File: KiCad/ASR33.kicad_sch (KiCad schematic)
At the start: 45 parts, among them J1 USB-C, J2 DC, J3 Power, J4 RUN, J5 Tx, J6 Rx, Q1 NX7002AK, SW1 SW_Push, U1 FT231XQ, U2 ESP32-WROOM-32, U3 NCR402U, U4 NCR402U, U5 LTV-356T, U6 LMR16006+FB, U7 QR

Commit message: New PICO version
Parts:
- removed JP1, JP2, JP4: 20R NF, RevK:Pad_1206_0805_Open, symbol Jumper:SolderJumper_2_Open
- removed JP3: GND-Linked, RevK:Pad_1206_0805_Bridged, symbol Jumper:SolderJumper_2_Bridged
- removed U2: ESP32-WROOM-32, RevK:ESP32-WROOM-32, symbol RevK:ESP32-WROOM-32
- added U1: ESP32-PICO-MINI-02, RevK:ESP32-PICO-MINI-02, symbol RevK:ESP32-PICO-MINI-02
- renumbered U1 to U2
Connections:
- net +3V3: now also U1.3 (3V3)
- net B: now also U1.15 (IO25)
- net BUTTON: now also U1.26 (IO20)
- net EN: now also U1.8 (EN)
- net G: now also U1.13 (IO33)
- net GND: now also U1.1 (GND), U1.11 (GND), U1.14 (GND), U1.2 (GND), U1.36 (GND), U1.37 (GND), U1.38 (GND), U1.39 (GND), U1.40 (GND), U1.41 (GND), U1.42 (GND), U1.43 (GND), U1.44 (GND), U1.45 (GND), U1.46 (GND), U1.47 (GND), U1.48 (GND), U1.49 (GND), U1.50 (GND), U1.51 (GND), U1.52 (GND), U1.53 (GND)
- net GPIO0: now also U1.23 (IO0)
- net I: now also U1.30 (RXD0)
- net MTR: now also U1.34 (IO22)
- net O: now also U1.31 (TXD0)
- net PWR: now also U1.35 (IO21)
- net R: now also U1.12 (IO32)
- net RUN: now also U1.33 (IO19)
- net RX20MA: now also U1.16 (IO26)
- net TX20MA: now also U1.17 (IO27)
- net CHARGER: no longer names the net of U2.14 (CBUS1)
- net USB: no longer names the net of U2.15 (CBUS0)
- no-connect marks 21 -> 8
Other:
- moved on the sheet: R1

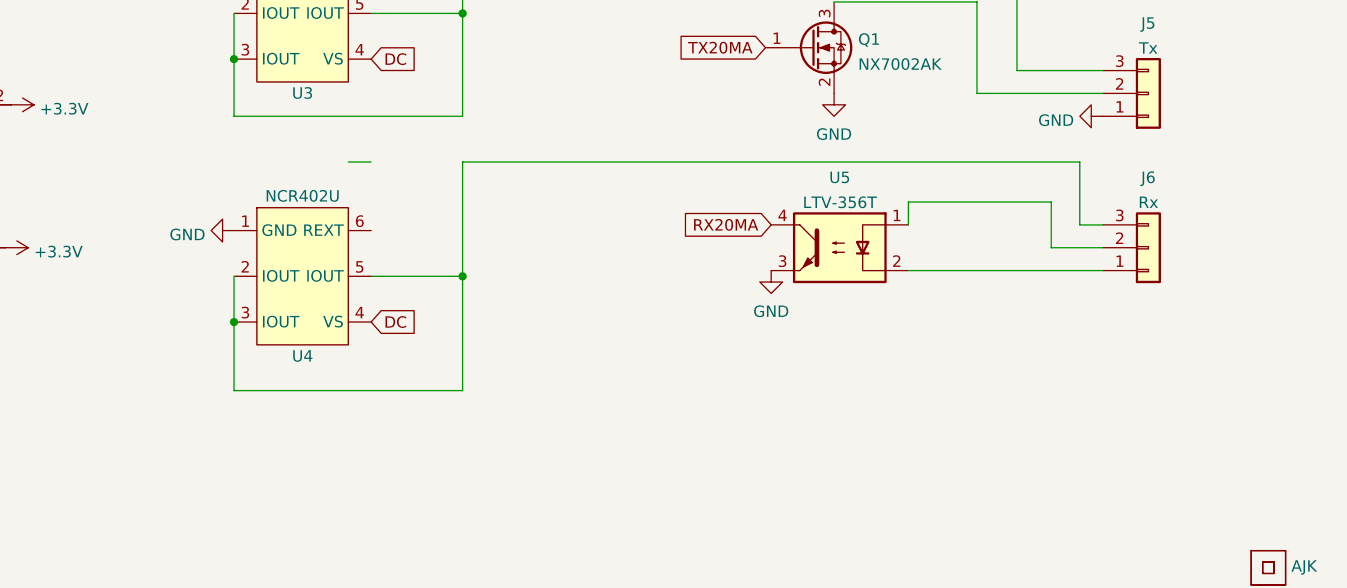
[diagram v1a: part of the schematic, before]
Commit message: Reinstated the GND link
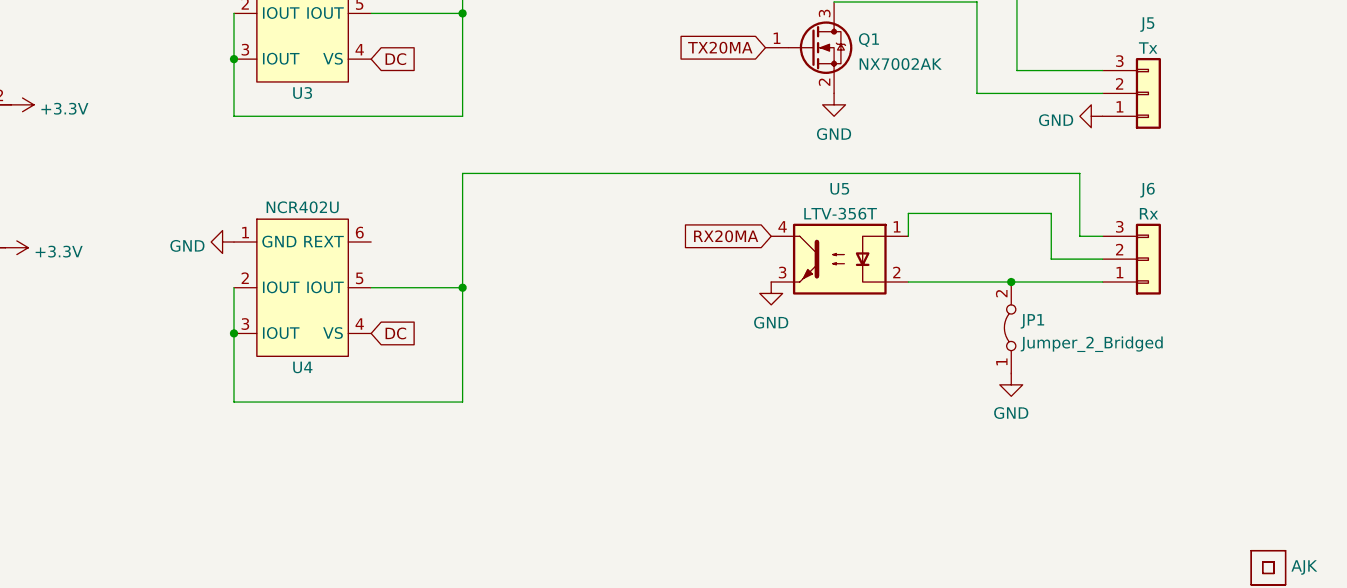
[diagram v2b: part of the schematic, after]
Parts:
- added JP1: Jumper_2_Bridged, RevK:Pad_1206_0805_Bridged, symbol Jumper:Jumper_2_Bridged
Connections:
- net GND: now also JP1.1 (A)
- net at J6.1 (Pin_1), U5.2: now also JP1.2 (B)
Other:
- moved on the sheet: J6, U4, U5

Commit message: Tidy up
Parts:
- J1: symbol Connector:USB_C_Receptacle_USB2.0 -> RevK:USB-C
- J2: symbol Connector_Generic:Conn_01x02 -> RevK:PowerIn
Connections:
- no-connect marks 8 -> 20
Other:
- moved on the sheet: U3, U4
